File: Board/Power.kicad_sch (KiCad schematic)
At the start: 76 parts

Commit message: more work on r2.1a - only bom xls is missing/outdated
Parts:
- C121: value 1u -> 0.1u
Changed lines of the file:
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@@
 			)
 		)
-		(property "Value" "1u"
+		(property "Value" "0.1u"
 			(at 131.064 152.019 0)
 			(effects

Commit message: first try on BOM
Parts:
- removed C38: 22u, csa_ultracpu:E2,5-6, symbol csa_ultracpu-eagle-import:CPOL-EUE2.5-6
- added C38: 22u, csa_ultracpu:C0805, symbol csa_ultracpu-eagle-import:C-EUC0805
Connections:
- net GND: now also C38.2
- net V33: now also C38.1
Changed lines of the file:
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@@
-	)
-	(symbol
-		(lib_id "csa_ultracpu-eagle-import:CPOL-EUE2.5-6")
-		(at 129.54 175.26 0)
-		(unit 1)
-		(exclude_from_sim no)
-		(in_bom yes)
-		(on_board yes)
-		(dnp no)
-		(property "Reference" "C38"
-			(at 130.683 174.7774 0)
-			(effects
-				(font
-					(size 1.778 1.5113)
-				)
-				(justify left bottom)
-			)
-		)
-		(property "Value" "22u"
-			(at 130.683 179.8574 0)
-			(effects
-				(font
-					(size 1.778 1.5113)
-				)
-				(justify left bottom)
-			)
-		)
-		(property "Footprint" "csa_ultracpu:E2,5-6"
-			(at 129.54 175.26 0)
-			(effects
-				(font
-					(size 1.27 1.27)
-				)
-				(hide yes)
-			)
-		)
-		(property "Datasheet" ""
-			(at 129.54 175.26 0)
-			(effects
-				(font
-					(size 1.27 1.27)
-				)
-				(hide yes)
-			)
-		)
-		(property "Description" ""
-			(at 129.54 175.26 0)
-			(effects
-				(font
-					(size 1.27 1.27)
-				)
-				(hide yes)
-			)
-		)
-		(pin "+"
-		)
-		(pin "-"
-		)
-		(instances
-			(project ""
-				(path "/381336a5-a662-4c84-a650-90475fa59a97/9a31233f-ca04-4c2c-b272-c5e144bd19b1"
-					(reference "C38")
-					(unit 1)
-				)
-			)
-		)
 	)
 	(symbol
@@
 					(unit 1)
 				)
+			)
+		)
+	)
+	(symbol
+		(lib_id "csa_ultracpu-eagle-import:C-EUC0805")
+		(at 129.54 175.26 0)
+		(unit 1)
+		(exclude_from_sim no)
+		(in_bom yes)
+		(on_board yes)
+		(dnp no)
+		(property "Reference" "C38"
+			(at 131.064 174.879 0)
+			(effects
+				(font
+					(size 1.778 1.5113)
+				)
+				(justify left bottom)
+			)
+		)
+		(property "Value" "22u"
+			(at 131.064 179.959 0)
+			(effects
+				(font
+					(size 1.778 1.5113)
+				)
+				(justify left bottom)
+			)
+		)
+		(property "Footprint" "csa_ultracpu:C0805"
+			(at 129.54 175.26 0)
+			(effects
+				(font
+					(size 1.27 1.27)
+				)
+				(hide yes)
+			)
+		)
+		(property "Datasheet" ""
+			(at 129.54 175.26 0)
+			(effects
+				(font
+					(size 1.27 1.27)
+				)
+				(hide yes)
+			)
+		)
+		(property "Description" ""
+			(at 129.54 175.26 0)
+			(effects
+				(font
+					(size 1.27 1.27)
+				)
+				(hide yes)
+			)
+		)
+		(pin "1"
+		)
+		(pin "2"
+		)
+		(instances
+			(project "csa_ultracpu"
+				(path "/381336a5-a662-4c84-a650-90475fa59a97/9a31233f-ca04-4c2c-b272-c5e144bd19b1"
+					(reference "C38")
+					(unit 1)
+				)

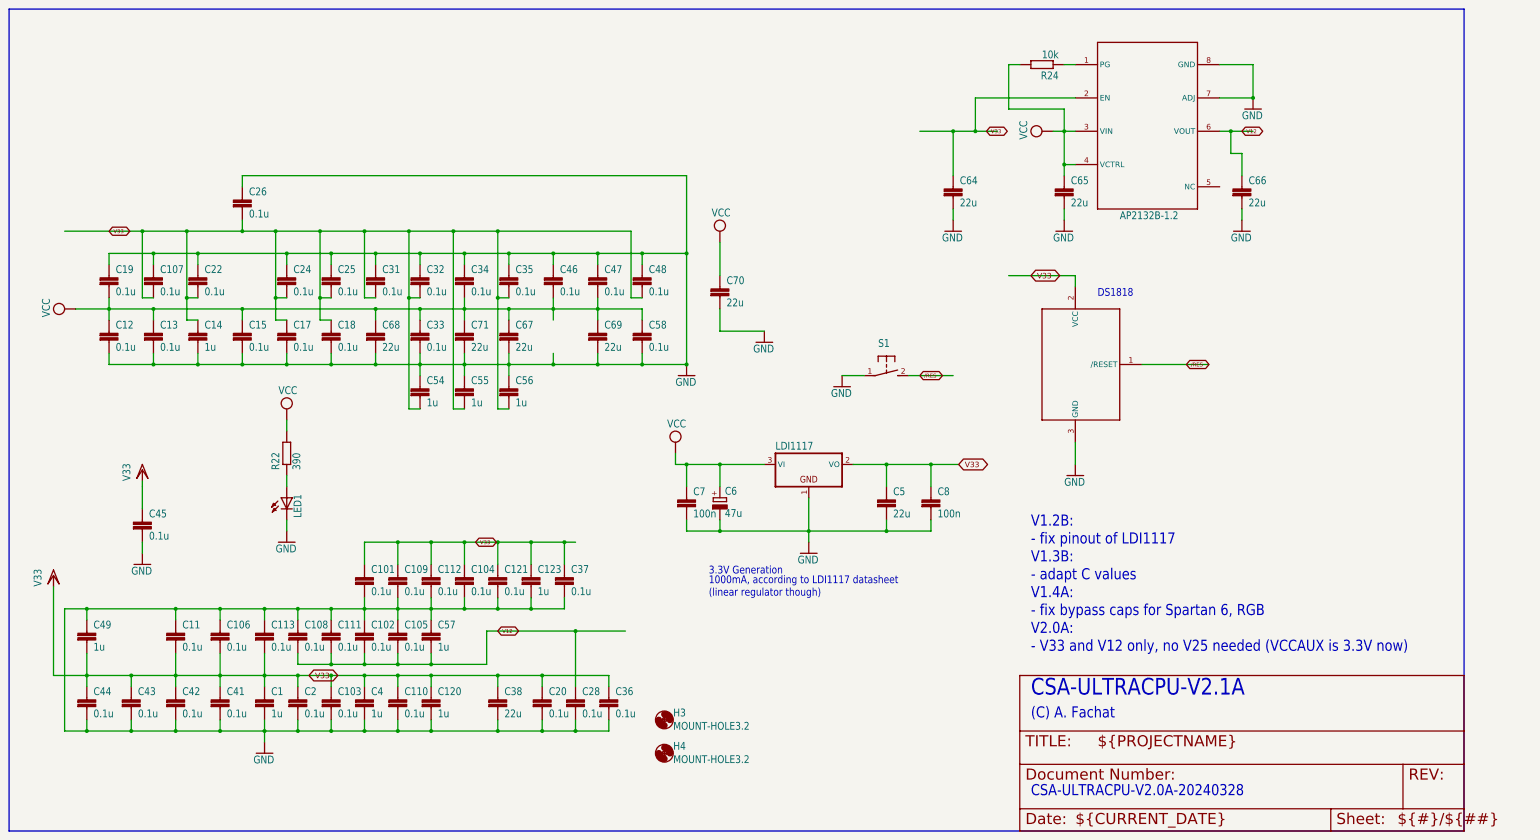
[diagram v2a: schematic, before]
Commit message: start r2.2a, moving from VGA to HDMI
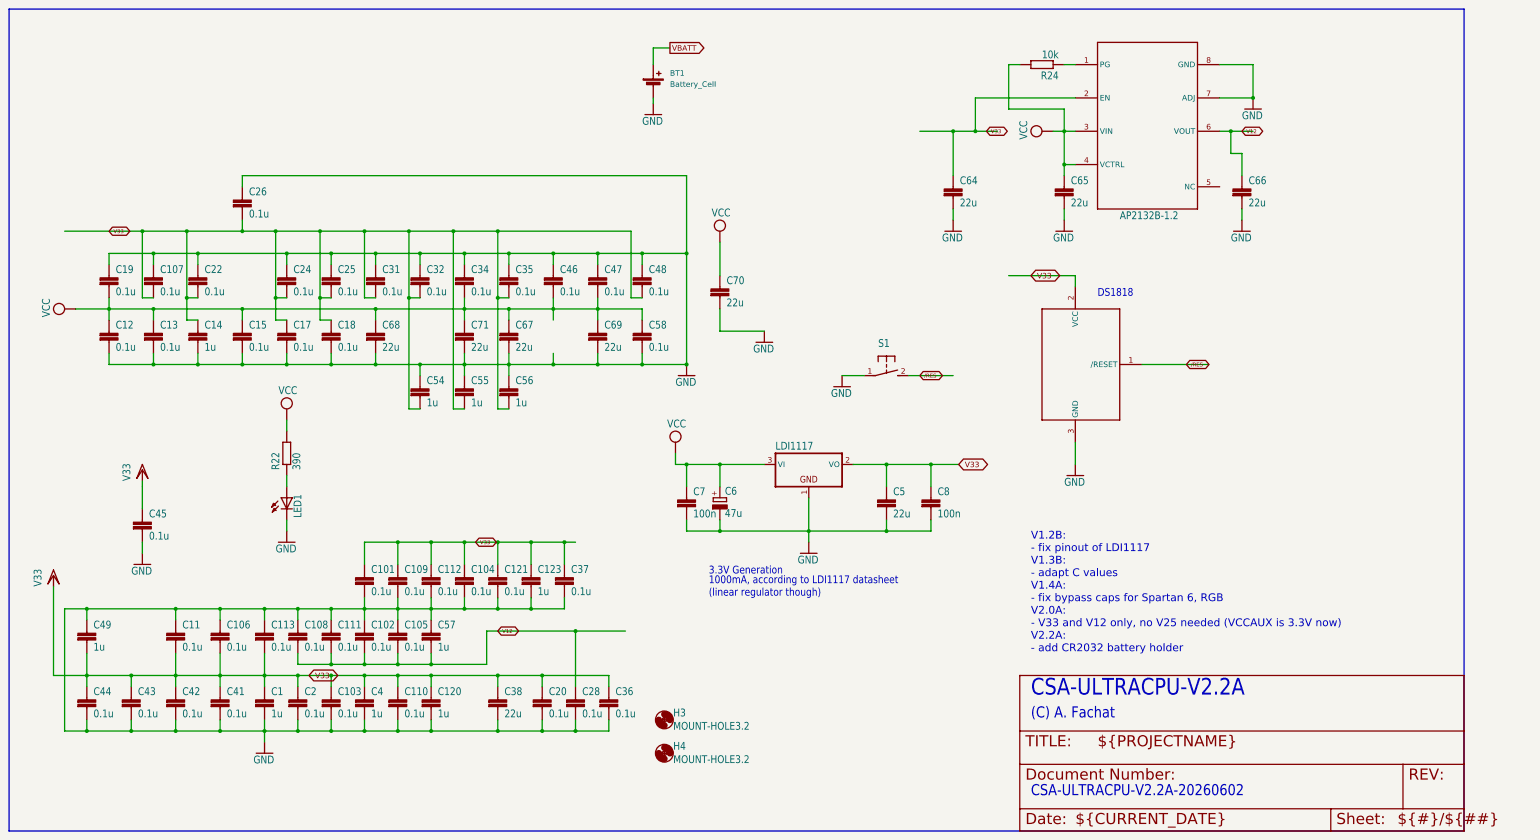
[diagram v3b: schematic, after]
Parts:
- removed C33: 0.1u, csa_ultracpu:C0603, symbol csa_ultracpu-eagle-import:C-EUC0603
- added BT1: Battery_Cell, csa_ultracpu:Kinghelm CR2032 Holder, symbol Device:Battery_Cell
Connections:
- net GND: now also BT1.2 (-)
- new net VBATT: BT1.1 (+)
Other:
- note added: "CSA-ULTRACPU-V2.2A"
- note added: "CSA-ULTRACPU-V2.2A-20260602"
- note added: "V1.2B: - fix pinout of LDI1117 V1.3B: - adapt C values V1.4A: - fix bypass caps for Spartan 6, RGB V2.0A: - V33 and V12 only, no V25 needed (VCCAUX is 3.3V now) V2.2A: - add CR2032 battery holder"
- note removed: "CSA-ULTRACPU-V2.0A-20240328"
- note removed: "CSA-ULTRACPU-V2.1A"
- note removed: "V1.2B: - fix pinout of LDI1117 V1.3B: - adapt C values V1.4A: - fix bypass caps for Spartan 6, RGB V2.0A: - V33 and V12 only, no V25 needed (VCCAUX is 3.3V now)"
